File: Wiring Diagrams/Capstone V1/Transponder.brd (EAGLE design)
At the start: 62.5 x 53.5 mm, 15 parts, among them J1 ARD_H1, J2 ARD_H2, U1 LLC, U2 MIC5211-LXYM6-TR

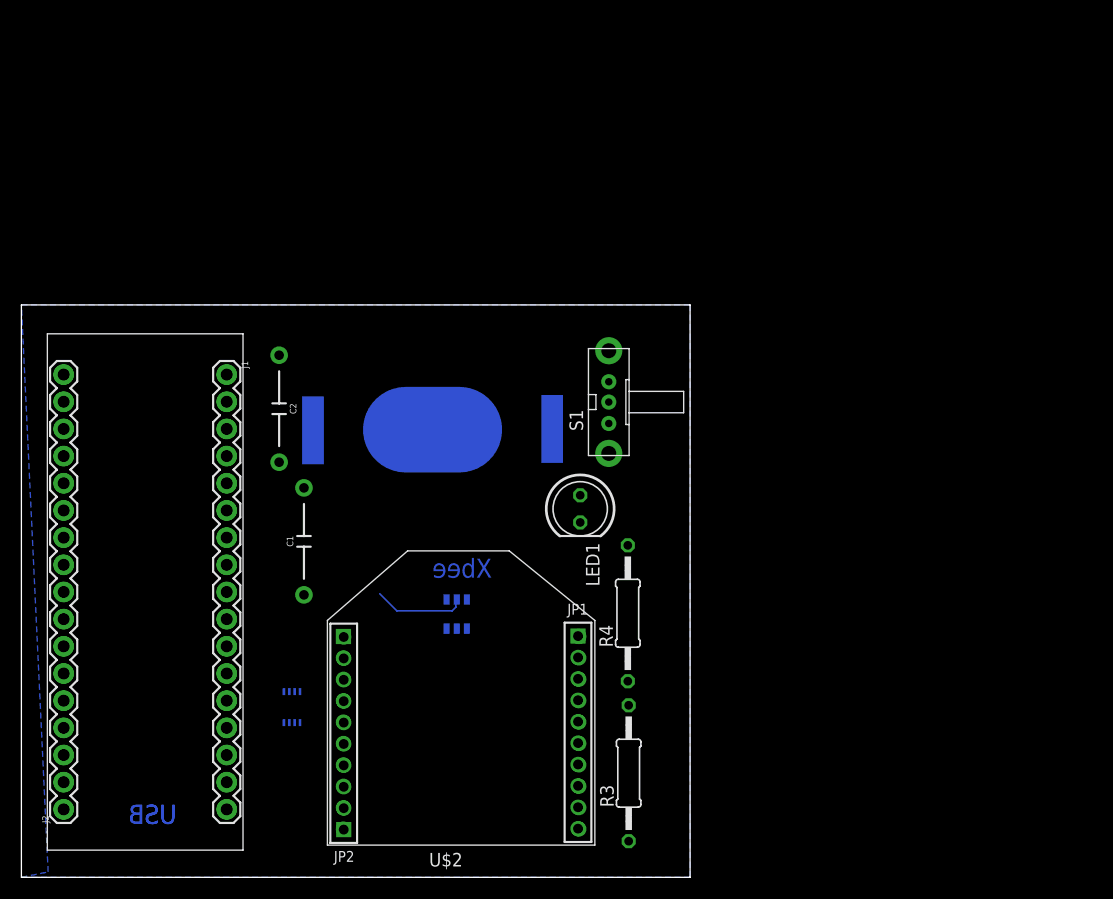
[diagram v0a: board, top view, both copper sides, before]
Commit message: Added datasheets, made transponder pcb files
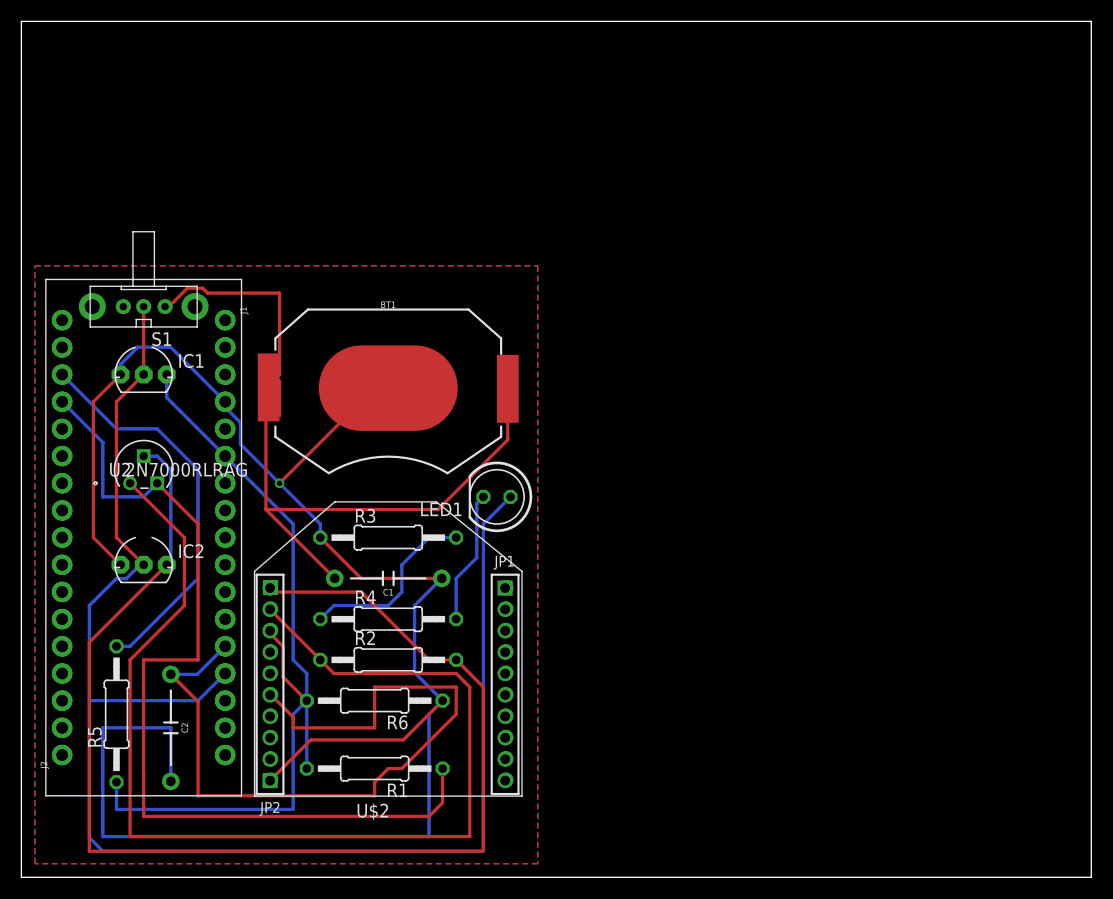
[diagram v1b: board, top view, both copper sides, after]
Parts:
- removed U1: LLC, adafruit:VFSOP-8
- added FRAME1: FRAME-LETTERNO_PACKAGE, SparkFun-Aesthetics:DUMMY
- added IC1: MCP1700-5002E/TO-ND, adafruit:TO92-INLINE
- added IC2: MCP1700-3302E/TO-ND, adafruit:TO92-INLINE
- added R1, R2, R6: 10k, resistor:0207/12
- added R5: 4.7k, resistor:0207/12
- J1, J2: device SparkFun-Connectors:1X17 -> SparkFun-Connectors:1X17_NO_SILK
- U2: value MIC5211-LXYM6-TR -> 2N7000RLRAG; device MIC5211-LXYM6-TR:SOT-23-6_M6 -> 2N7000RLRAG:TO-92
- moved S1 44.4 mm to (11.4, 53.3), turned to 180 degrees
- moved U2 31.6 mm to (12.7, 39.4), flipped to the top, turned to 0 degrees
- moved C2 31.5 mm to (14.0, 14.0)
- moved R3 31.5 mm to (34.3, 31.8), turned to 0 degrees
- moved R4 22.4 mm to (34.3, 24.1), turned to 0 degrees
- moved C1 8.61 mm to (34.3, 27.9), turned to 180 degrees
- moved JP2 8.27 mm to (23.2, 18.0)
- moved U$2 8.21 mm to (34.3, 21.6)
- moved JP1 8.15 mm to (45.2, 18.0)
- moved LED1 7.86 mm to (44.5, 35.6), turned to 180 degrees
- moved BT1 5.67 mm to (34.3, 45.7), flipped to the top, turned to 0 degrees
- moved J2 5.08 mm to (3.81, 11.4)
- moved J1 5.08 mm to (19.1, 52.1)
- moved U$1 5.08 mm to (11.4, 31.8)
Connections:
- net N$48 renamed RSSI
- new net N$2: JP2.3, U$2.8
- net 3.3V: now also IC2.3, R2.2, U2.2; no longer U1.P$3, U1.P$6, U2.6
- net 5V: now also IC1.3, R1.2; no longer U1.P$7, U2.4
- net DIN: now also R5.1, R6.2; no longer U1.P$5
- net DOUT: now also R2.1, U2.1; no longer U1.P$4
- net GND: now also IC1.1, IC2.1, R6.1; no longer U1.P$2, U2.2
- net RXA: now also R1.1, U2.3; no longer U1.P$1
- net TXA: now also R5.2; no longer U1.P$8
- net V_BATT: now also IC1.2, IC2.2; no longer U2.1, U2.3, U2.5
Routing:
- net GND: track 8.66 -> 174.6 mm, vias 0 -> 1
- net V_BATT: track 0.00 -> 139.9 mm
- net 3.3V: track 0.00 -> 117.8 mm
- net DOUT: track 0.00 -> 104.6 mm
- net RXA: track 0.00 -> 85.6 mm
- net N$1: track 0.00 -> 79.0 mm
- net RSSI: track 0.00 -> 72.2 mm
- net 5V: track 0.00 -> 42.2 mm
- net DIN: track 0.00 -> 37.7 mm
- net TXA: track 0.00 -> 36.8 mm
- net N$5: track 0.00 -> 17.3 mm
- net N$4: track 0.00 -> 12.5 mm
- added copper zone on layer 1, net GND
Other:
- board size 62.5 x 53.5 mm -> 100 x 80 mm
- board text removed: "USB"
- board text removed: "Xbee"
